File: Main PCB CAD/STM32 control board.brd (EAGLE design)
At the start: 120 x 104 mm, 165 parts, among them J1 B3B-PH, J10 B3B-PH, J11 B3B-PH, J12 B3B-PH, J13 B3B-PH, J14 B6B-PH, J15 DG301-4P, J2 B3B-PH, J3 B4B-PH, J4 B6B-PH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

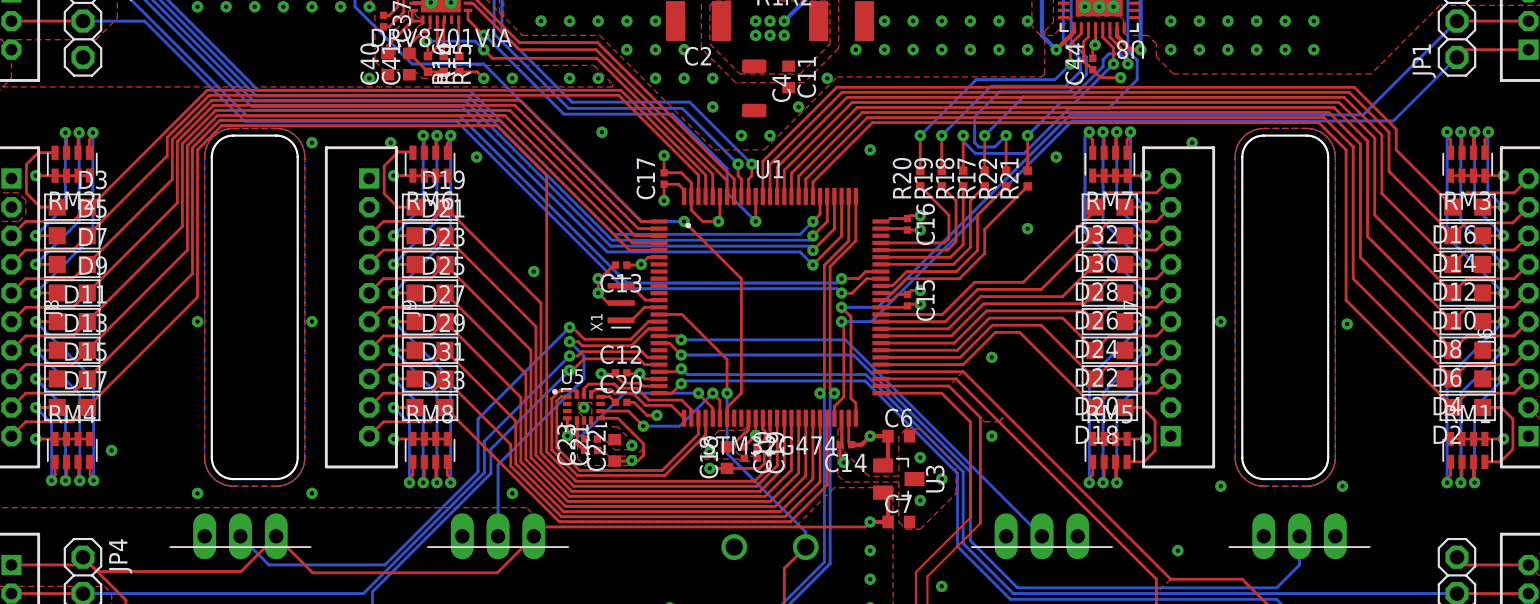
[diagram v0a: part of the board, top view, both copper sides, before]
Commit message: Added some changes to routing
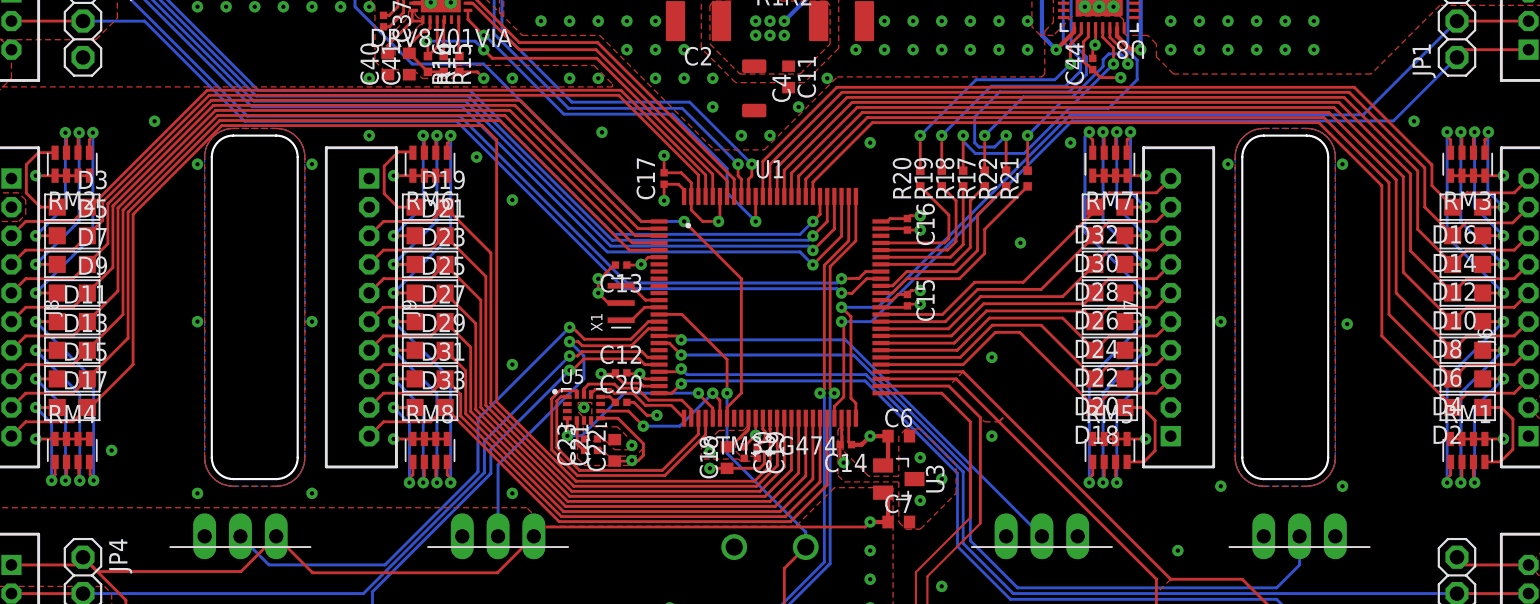
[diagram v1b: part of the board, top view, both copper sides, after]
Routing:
- net GND: vias 223 -> 228

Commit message: silkscreen
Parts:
- moved J1 0.36 mm to (78.8, 92.2)
- moved C32 0.20 mm to (52.2, 82.0)
- renumbered PAD1 to POS, PAD2 to NEG
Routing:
- net +3V3: track 601.0 -> 599.6 mm
